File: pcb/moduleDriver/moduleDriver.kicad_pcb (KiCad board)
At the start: 2 copper layers, 70 x 80 mm, 44 parts, among them J1 MOTOR, J10 Sensor, J11 Power, J12 Power, J13 Power, J2 MOTOR, J3 MOTOR, J4 MOTOR, J5 IDC, J6 IDC, J7 Sensor, J8 Sensor, J9 Sensor, U1 TPIC6B595, U2 TPIC6B595, U3 74HC165, U4 74HC125, U5 Raspberry Pi Pico, U6 OKI-78SR-5_1.5-W36-C, U7 HEF4104B

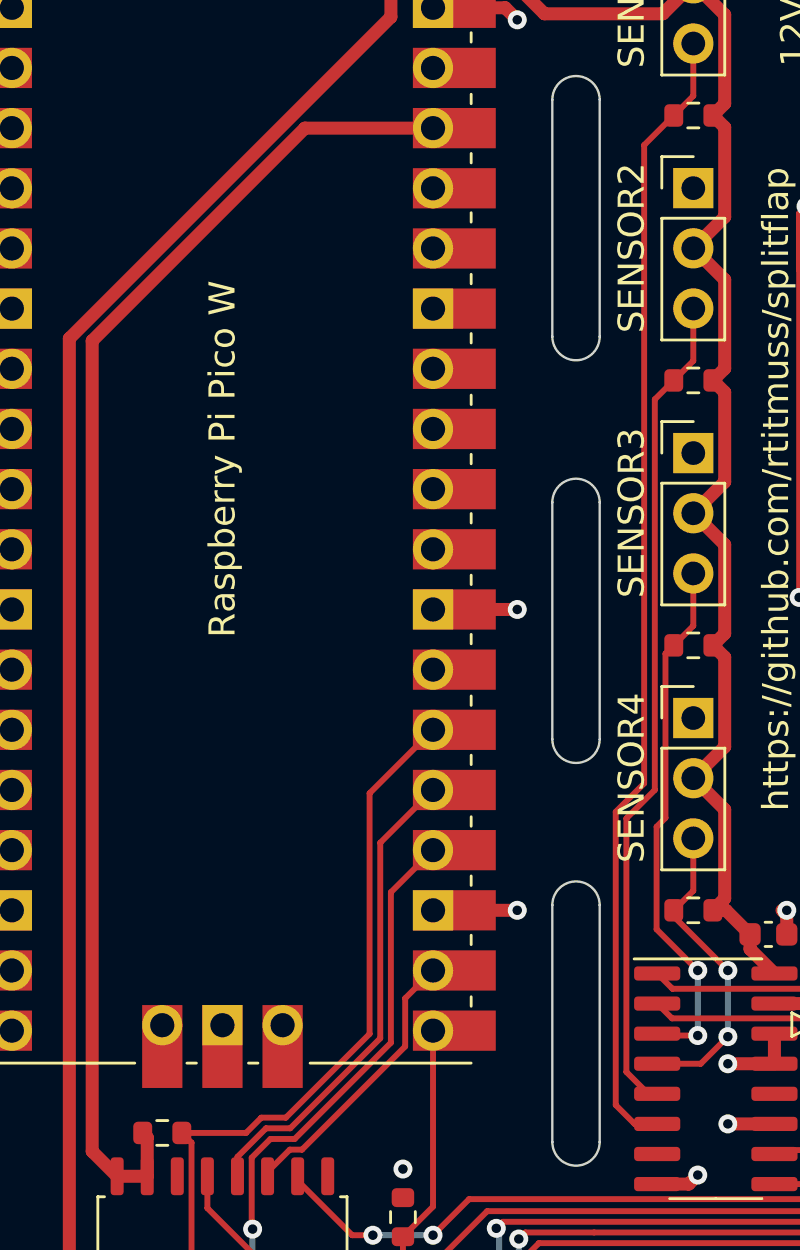
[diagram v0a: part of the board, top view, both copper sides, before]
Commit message: Back silkscreen
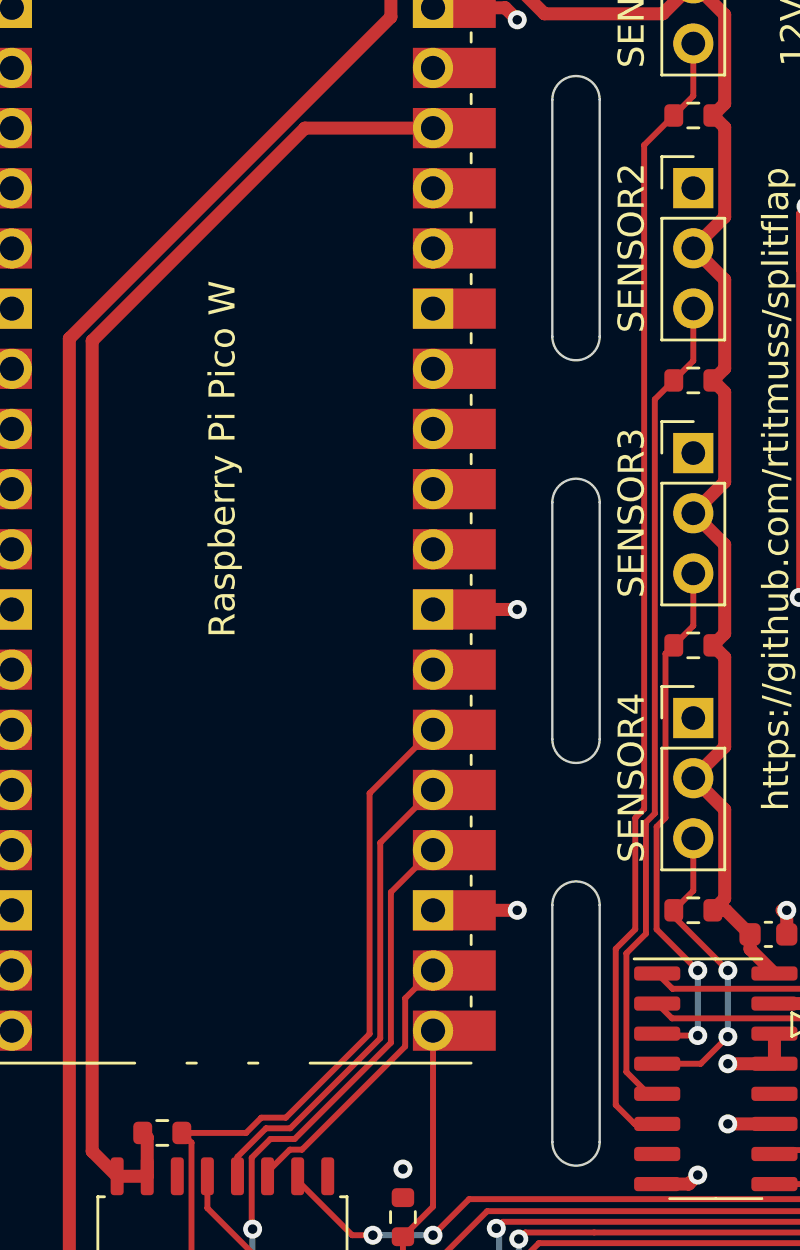
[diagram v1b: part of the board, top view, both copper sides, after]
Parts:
- added QR*****: github_qrcode, Library:github_qrcode, B.Cu at (84.3, 110.8)
- added QR*****: printables_qrcode, Library:printables_qrcode, B.Cu at (84.3, 83.2)
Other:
- board text added: "Designed for https://www.printables.com/ model/69464-split-flap-display by David Kingsman"

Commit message: Update schematic after review
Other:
- board text added: "Todo on the PCB: - Don't break the PCBs - Use two vias for ground where possible - Thick about thermal transfer - Pico antenna"
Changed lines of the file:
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@@
   (gr_arc (start 100 69) (mid 99 70) (end 98 69) (layer "Edge.Cuts") (width 0.1))
   (gr_line (start 100 69) (end 100 52) (layer "Edge.Cuts") (width 0.1))
+  (gr_text "Todo on the PCB:\n- Don't break the PCBs\n- Use two vias for ground where possible\n- Thick about thermal transfer\n- Pico antenna" (at 14.986 106.172) (layer "F.Cu")
+    (effects (font (size 1.5 1.5) (thickness 0.3)) (justify left))
+  )
   (gr_text "Designed for\nhttps://www.printables.com/\nmodel/69464-split-flap-display\nby David Kingsman\n" (at 120 61.976) (layer "B.SilkS")
     (effects (font (size 1.1 1.1) (thickness 0.15)) (justify mirror))

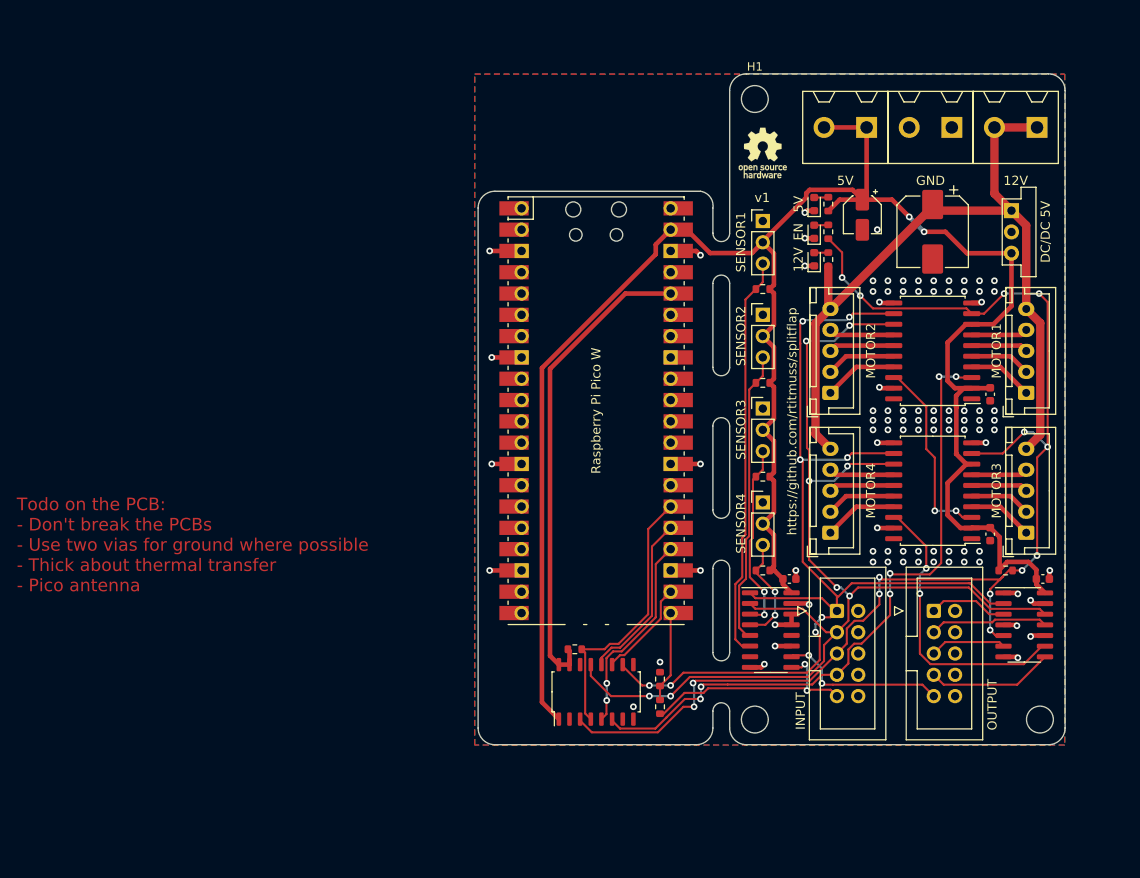
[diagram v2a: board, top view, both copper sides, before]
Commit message: Update footprints on PCB
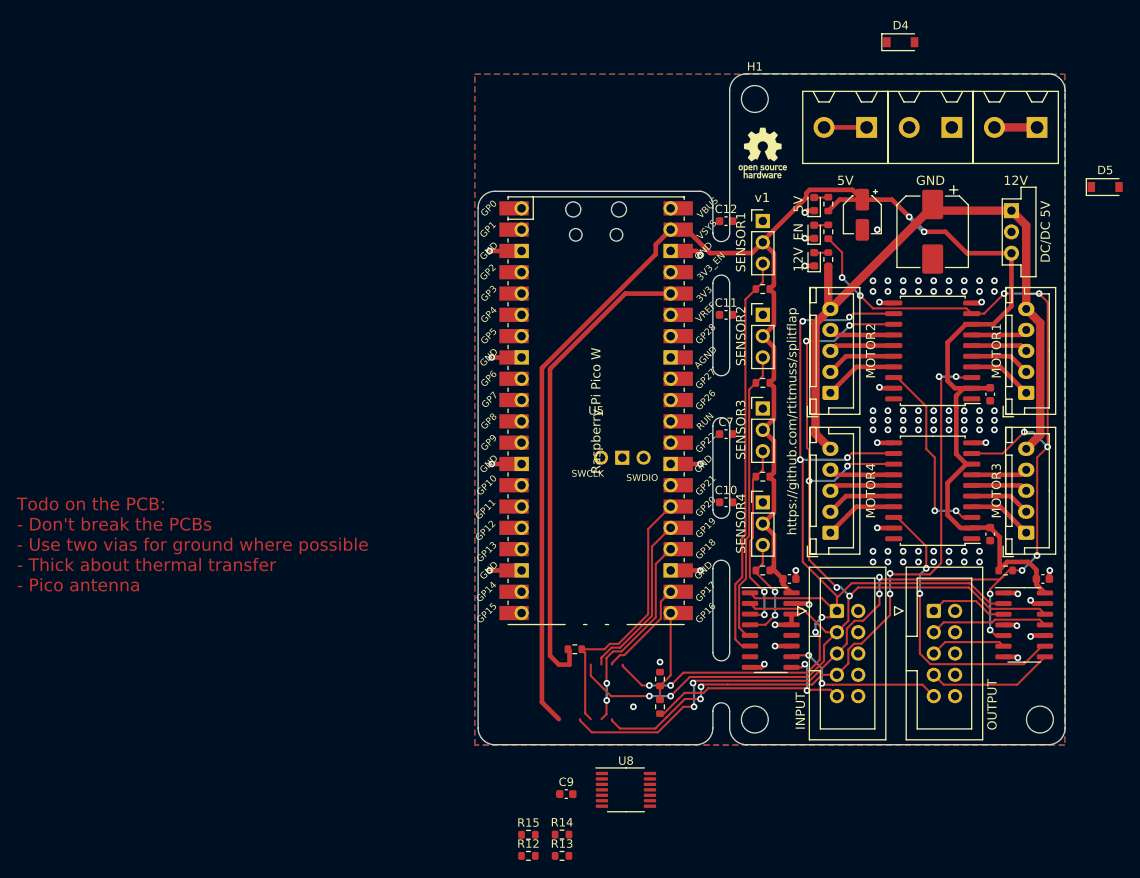
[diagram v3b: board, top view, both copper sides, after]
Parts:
- removed U7: HEF4104B, Package_SO:SOIC-16_4.55x10.3mm_P1.27mm
- added C10: 1uF, Capacitor_SMD:C_0603_1608Metric, F.Cu at (99.6, 101.1)
- added C11: 1uF, Capacitor_SMD:C_0603_1608Metric, F.Cu at (99.6, 78.7)
- added C12: 1uF, Capacitor_SMD:C_0603_1608Metric, F.Cu at (99.6, 67.6)
- added C7: 1uF, Capacitor_SMD:C_0603_1608Metric, F.Cu at (99.6, 93.0)
- added C9: 1uF, Capacitor_SMD:C_0603_1608Metric, F.Cu at (80.5, 135.9)
- added D4: B5819W, Diode_SMD:D_SOD-123, F.Cu at (120.4, 46.2)
- added D5: B5819W, Diode_SMD:D_SOD-123, F.Cu at (144.8, 63.5)
- added R12: 5.1k, Resistor_SMD:R_0603_1608Metric, F.Cu at (76.0, 143.3)
- added R13: 5.1k, Resistor_SMD:R_0603_1608Metric, F.Cu at (80.0, 143.3)
- added R14: 5.1k, Resistor_SMD:R_0603_1608Metric, F.Cu at (80.0, 140.7)
- added R15: 5.1k, Resistor_SMD:R_0603_1608Metric, F.Cu at (76.0, 140.7)
- added U8: 74AHCT125, Package_SO:TSSOP-14_4.4x5mm_P0.65mm, F.Cu at (87.6, 135.4)
- R1: value 200R -> 2.4k
- R2, R3: value 510R -> 1.2k
- U5: value Raspberry Pi Pico -> PicoW; footprint MCU_RaspberryPi_and_Boards:RPi_Pico_SMD_TH -> Library:RPi_PicoW_SMD_TH
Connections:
- J11 pad 1: +12V -> Net-(D5-Pad2)
- J11 pad 2: +12V -> Net-(D5-Pad2)
- U6 pad 3: +5V -> Net-(D4-Pad2)
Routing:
- net +12V: track 96.9 -> 81.1 mm
- net +5V: track 245.2 -> 236.4 mm
- net Net-(D5-Pad2): track 0.00 -> 5.08 mm

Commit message: Fix pull up/downs on buffer
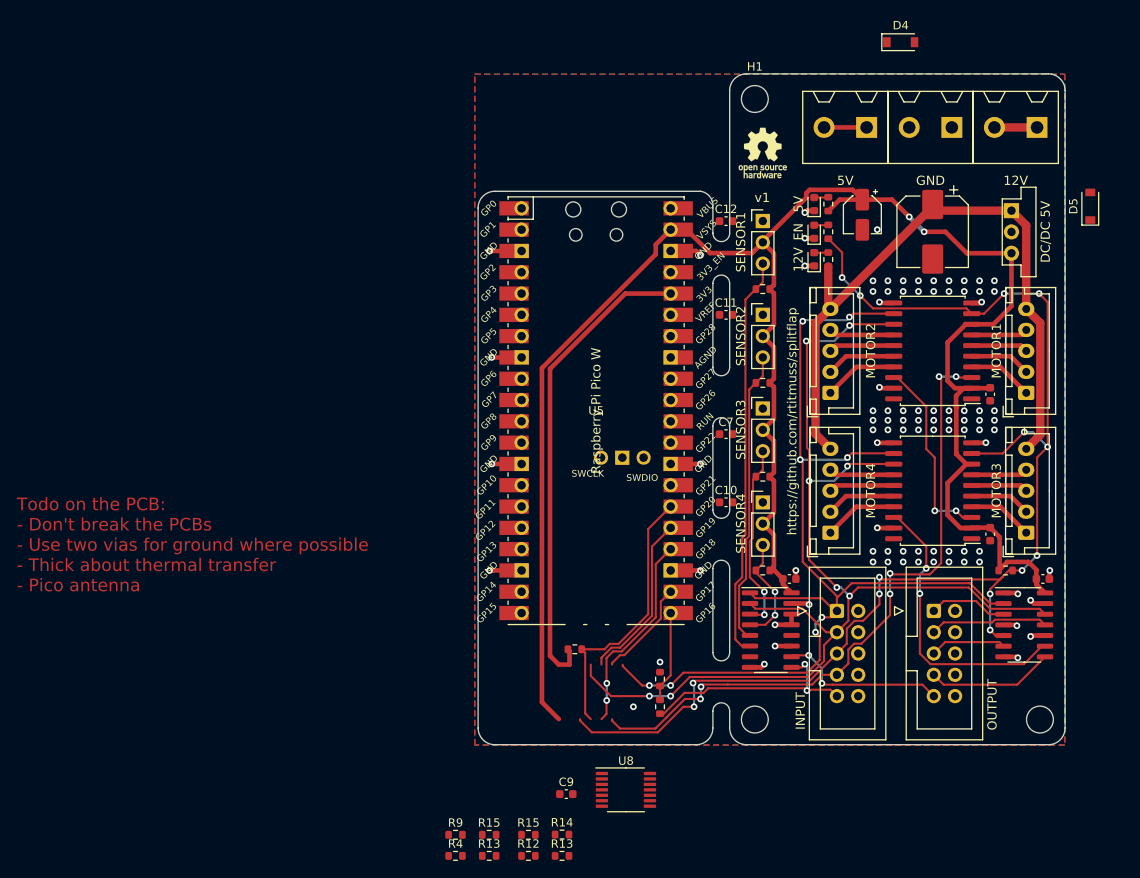
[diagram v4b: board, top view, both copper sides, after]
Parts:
- added R13: 100k, Resistor_SMD:R_0603_1608Metric, F.Cu at (71.3, 143.3)
- added R15: 100k, Resistor_SMD:R_0603_1608Metric, F.Cu at (71.3, 140.7)
- added R4: 100k, Resistor_SMD:R_0603_1608Metric, F.Cu at (67.3, 143.3)
- added R9: 100k, Resistor_SMD:R_0603_1608Metric, F.Cu at (67.3, 140.7)
- R12, R14: value 5.1k -> 100k
- moved D5 2.90 mm to (143.0, 65.8), turned to 90 degrees
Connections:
- net /PWR_ENABLE_OUT renamed /~{PWR_ENABLE_OUT}
- D3 pad 1: GND -> /~{PWR_ENABLE_IN}
- J5 pad 5: /PWR_ENABLE_IN -> /~{PWR_ENABLE_IN}
- R12 pad 2: /MOTOR_IN_3V3 -> /LATCH_IN_3V3
- R14 pad 1: GND -> /~{PWR_ENABLE_IN}
- R14 pad 2: /CLOCK_IN_3V3 -> +5V
- R3 pad 1: /PWR_ENABLE_IN -> +5V
- U1 pad 9: /PWR_ENABLE_IN -> /~{PWR_ENABLE_IN}
- U2 pad 9: /PWR_ENABLE_IN -> /~{PWR_ENABLE_IN}
- U4 pad 5: /PWR_ENABLE_IN -> /~{PWR_ENABLE_IN}
- U5 pad 26: /PWR_ENABLE_IN_3V3 -> /~{PWR_ENABLE_IN_3V3}
- U5 pad 27: unconnected-(U5-Pad27) -> /~{BUFFER_ENABLE_3V3}
- U8 pad 1: GND -> /~{BUFFER_ENABLE_3V3}
- U8 pad 10: GND -> /~{BUFFER_ENABLE_3V3}
- U8 pad 11: /CLOCK_IN -> /LATCH_IN
- U8 pad 12: /CLOCK_IN_3V3 -> /LATCH_IN_3V3
- U8 pad 13: GND -> /~{BUFFER_ENABLE_3V3}
- U8 pad 2: /PWR_ENABLE_IN_3V3 -> /~{PWR_ENABLE_IN_3V3}
- U8 pad 3: /PWR_ENABLE_IN -> /~{PWR_ENABLE_IN}
- U8 pad 4: GND -> /~{BUFFER_ENABLE_3V3}
- U8 pad 8: /LATCH_IN -> /CLOCK_IN
- U8 pad 9: /LATCH_IN_3V3 -> /CLOCK_IN_3V3
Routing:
- net /~{PWR_ENABLE_IN}: track 0.00 -> 153.6 mm, vias 0 -> 15
- net /PWR_ENABLE_IN: track 152.5 -> 0.00 mm, vias 14 -> 0
- net /~{PWR_ENABLE_IN_3V3}: track 0.00 -> 32.4 mm
- net /PWR_ENABLE_IN_3V3: track 32.4 -> 0.00 mm
- net GND: track 59.7 -> 58.6 mm, vias 91 -> 90

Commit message: Updated layout
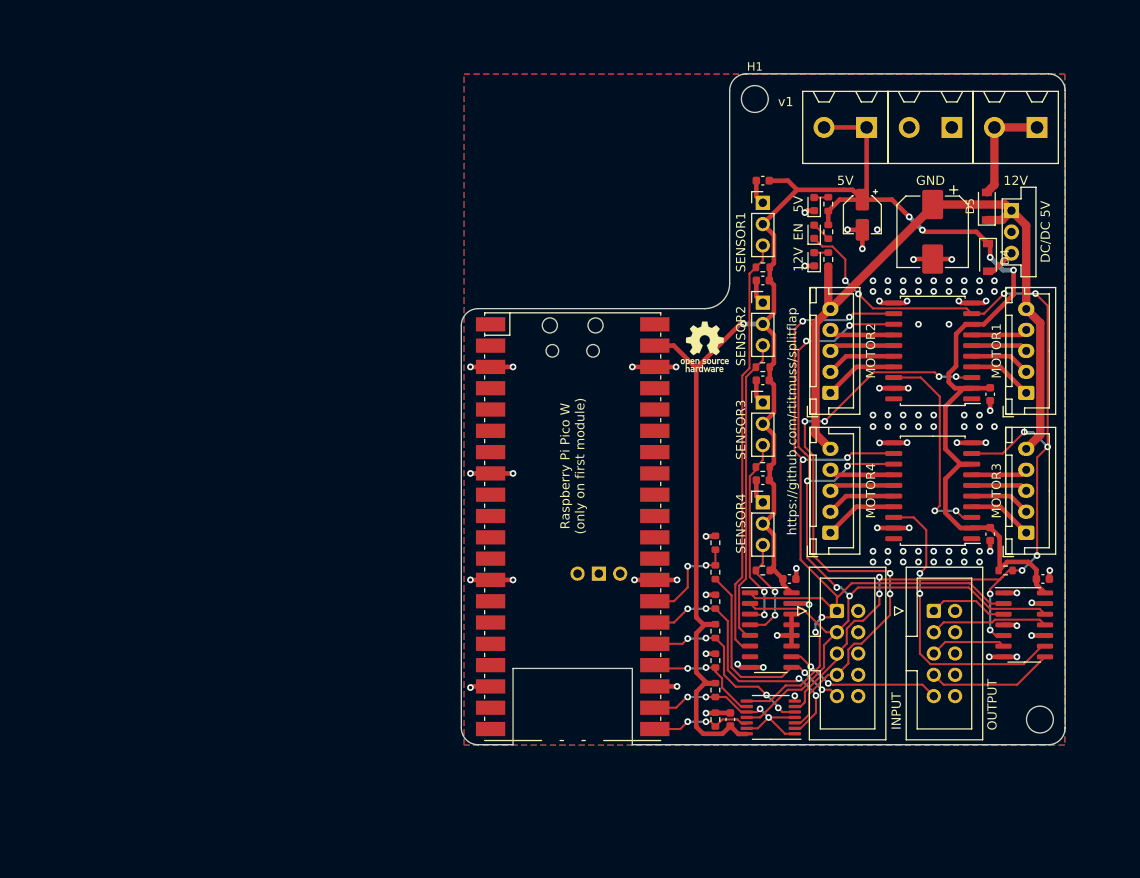
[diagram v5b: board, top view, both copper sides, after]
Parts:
- removed H2: MountingHole, MountingHole:MountingHole_3.2mm_M3_ISO7380
- removed the R13 at (80.0, 143.3)
- removed the R15 at (76.0, 140.7)
- removed the R4 at (132.9, 109.2)
- removed the R9 at (81.5, 118.6)
- moved R14 61.6 mm to (132.9, 109.2), turned to 180 degrees
- moved R9 39.4 mm to (98.3, 116.5), turned to 90 degrees
- moved R12 37.6 mm to (98.3, 112.9), turned to -90 degrees
- moved R13 35.6 mm to (98.3, 120.0), turned to -90 degrees
- moved R4 35.0 mm to (98.3, 127.0), turned to -90 degrees
- moved R15 32.0 mm to (98.3, 123.5), turned to 90 degrees
- moved D4 27.7 mm to (130.8, 71.9), turned to -90 degrees
- moved REF** 24.1 mm to (97.0, 82.5)
- moved C9 21.5 mm to (100.1, 127.0), turned to 90 degrees
- moved U8 19.3 mm to (104.9, 126.7), turned to 180 degrees
- moved R10 17.5 mm to (98.3, 105.9)
- moved R11 17.4 mm to (98.3, 109.4)
- moved U5 14.1 mm to (81.3, 104.0)
- moved D5 12.3 mm to (130.7, 65.8)
- moved QR***** 10.7 mm to (81.3, 93.5)
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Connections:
- R12 pad 2: /LATCH_IN_3V3 -> /MOTOR_IN_3V3
- R4 pad 2: /LATCH_IN_3V3 -> /CLOCK_IN_3V3
- U5 pad 21: /SENSOR_OUT_3V3 -> /CLOCK_IN_3V3
- U5 pad 22: /LATCH_IN_3V3 -> /~{BUFFER_ENABLE_3V3}
- U5 pad 24: /MOTOR_IN_3V3 -> /LATCH_IN_3V3
- U5 pad 25: /CLOCK_IN_3V3 -> /~{PWR_ENABLE_IN_3V3}
- U5 pad 26: /~{PWR_ENABLE_IN_3V3} -> /MOTOR_IN_3V3
- U5 pad 27: /~{BUFFER_ENABLE_3V3} -> /SENSOR_OUT_3V3
- U5 pad 36: +3.3V -> unconnected-(U5-Pad36)
- U5 pad 42: unconnected-(U5-Pad42) -> GND
- U8 pad 11: /LATCH_IN -> /CLOCK_IN
- U8 pad 12: /LATCH_IN_3V3 -> /CLOCK_IN_3V3
- U8 pad 2: /~{PWR_ENABLE_IN_3V3} -> /MOTOR_IN_3V3
- U8 pad 3: /~{PWR_ENABLE_IN} -> /MOTOR_IN
- U8 pad 5: /MOTOR_IN_3V3 -> /~{PWR_ENABLE_IN_3V3}
- U8 pad 6: /MOTOR_IN -> /~{PWR_ENABLE_IN}
- U8 pad 8: /CLOCK_IN -> /LATCH_IN
- U8 pad 9: /CLOCK_IN_3V3 -> /LATCH_IN_3V3
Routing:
- net +3.3V: track 57.0 -> 0.00 mm
- net GND: track 58.6 -> 108.5 mm, vias 90 -> 101
- net /~{PWR_ENABLE_IN}: track 153.6 -> 125.4 mm, vias 15 -> 12
- net /~{BUFFER_ENABLE_3V3}: track 0.00 -> 26.6 mm, vias 0 -> 4
- net /CLOCK_IN: track 132.9 -> 114.7 mm, vias 8 -> 6
- net /LATCH_IN: track 127.2 -> 112.9 mm, vias 8 -> 6
- net +5V: track 236.4 -> 248.4 mm, vias 2 -> 5
- net /MOTOR_IN_3V3: track 24.3 -> 34.1 mm, vias 2 -> 4
- net /~{PWR_ENABLE_IN_3V3}: track 32.4 -> 23.8 mm, vias 0 -> 4
- net Net-(D5-Pad2): track 5.08 -> 13.2 mm
- net /CLOCK_IN_3V3: track 20.3 -> 13.0 mm, vias 0 -> 2
- net /MOTOR_IN: track 79.1 -> 73.1 mm
- net Net-(D4-Pad2): track 0.00 -> 3.68 mm
- net +12V: track 81.1 -> 84.5 mm
- net /LATCH_IN_3V3: track 11.9 -> 15.2 mm, vias 0 -> 2
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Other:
- board size 70 x 80 mm -> 72 x 80 mm
- board text added: "Raspberry Pi Pico W (only on first module)"
- board text removed: "Raspberry Pi Pico W"
- board text removed: "Todo on the PCB: - Don't break the PCBs - Use two vias for ground where possible - Thick about thermal transfer - Pico antenna"
